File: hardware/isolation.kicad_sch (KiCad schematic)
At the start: 5 parts, among them IC2 UCC12040DVER

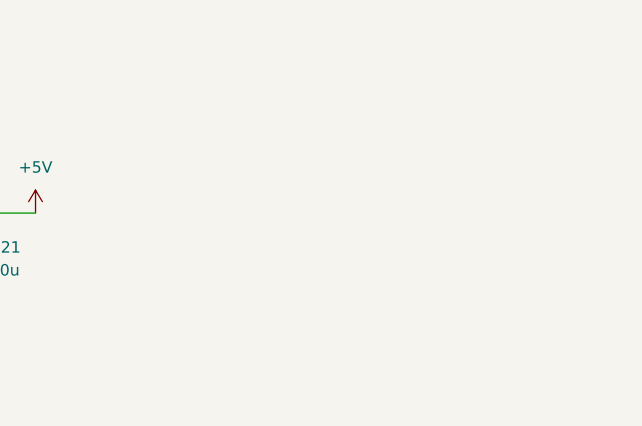
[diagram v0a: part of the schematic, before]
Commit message: Added 3V3-1 LDO
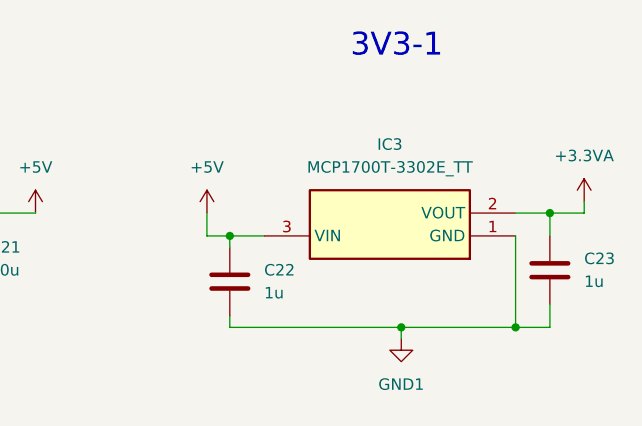
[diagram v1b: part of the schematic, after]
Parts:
- added C22, C23: 1u, Capacitor_SMD:C_0402_1005Metric, symbol Device:C
- added IC3: MCP1700T-3302E_TT, Stuttgart:SOT95P237X112-3N, symbol Stuttgart:MCP1700T-3302E_TT
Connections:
- net +5V: now also C22.1, IC3.3 (VIN)
- net GND1: now also C22.2, C23.2, IC3.1 (GND)
- new net +3.3VA: C23.1, IC3.2 (VOUT)
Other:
- note added: "3V3-1"

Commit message: Further ISO bridge development
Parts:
- added C24, C25: 100n, Capacitor_SMD:C_0402_1005Metric, symbol Device:C
- added IC4: ISO7742DBQR, Stuttgart:SOP64P600X175-16N, symbol Stuttgart:ISO7742DBQR
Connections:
- net +3.3VA: now also C25.1, IC4.10 (EN2), IC4.16 (VCC2)
- net GND: now also C24.2, IC4.2 (GND1_1), IC4.8 (GND1_2)
- net GND1: now also C25.2, IC4.15 (GND2_2), IC4.9 (GND2_1)
- new net +3V3: C24.1, IC4.1 (VCC1), IC4.7 (EN1)
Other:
- note added: "SPI Bridge 0"

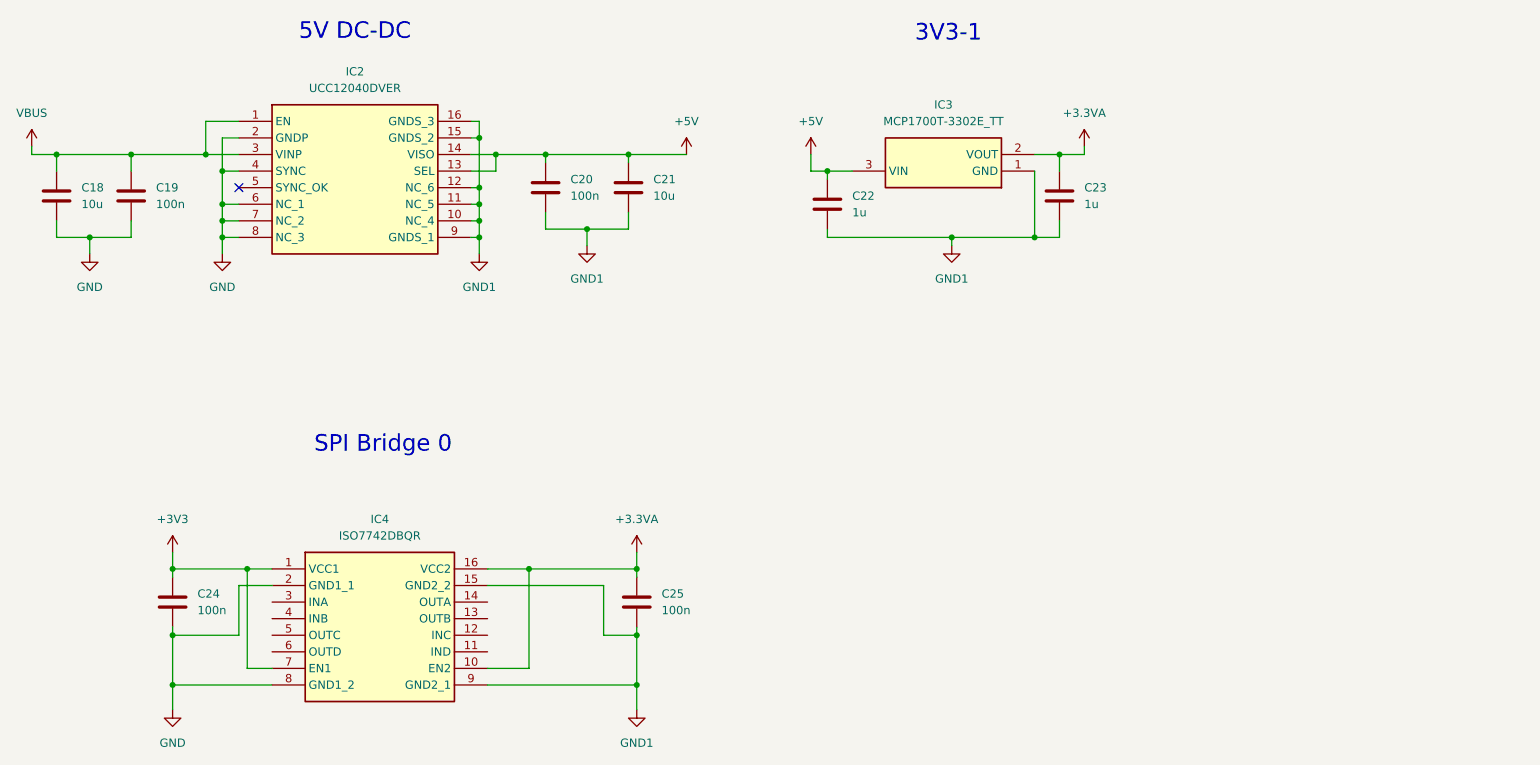
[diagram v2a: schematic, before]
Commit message: Isolation bridges complete
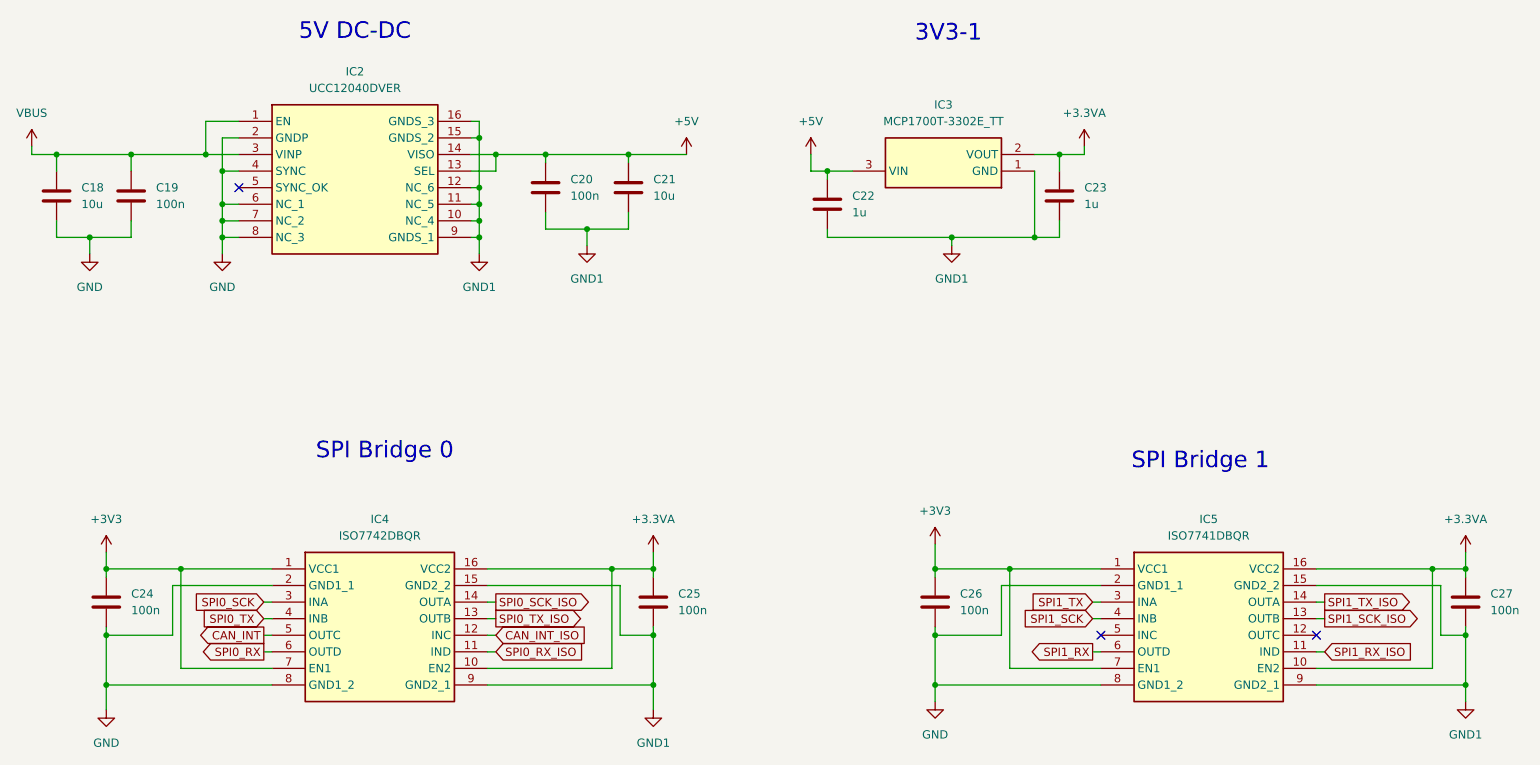
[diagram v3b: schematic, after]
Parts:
- added C26, C27: 100n, Capacitor_SMD:C_0402_1005Metric, symbol Device:C
- added IC5: ISO7741DBQR, Stuttgart:SOP64P600X175-16N, symbol Stuttgart:ISO7741DBQR
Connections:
- net +3.3VA: now also C27.1, IC5.10 (EN2), IC5.16 (VCC2)
- net +3V3: now also C26.1, IC5.1 (VCC1), IC5.7 (EN1)
- net GND: now also C26.2, IC5.2 (GND1_1), IC5.8 (GND1_2)
- net GND1: now also C27.2, IC5.15 (GND2_2), IC5.9 (GND2_1)
- net SPI0_RX_ISO: now reaches IC4.11 (IND)
- net CAN_INT_ISO: now reaches IC4.12 (INC)
- net SPI0_TX_ISO: now reaches IC4.13 (OUTB)
- net SPI0_SCK_ISO: now reaches IC4.14 (OUTA)
- net SPI0_SCK: now reaches IC4.3 (INA)
- net SPI0_TX: now reaches IC4.4 (INB)
- net CAN_INT: now reaches IC4.5 (OUTC)
- net SPI0_RX: now reaches IC4.6 (OUTD)
- new net SPI1_RX: IC5.6 (OUTD)
- new net SPI1_RX_ISO: IC5.11 (IND)
- new net SPI1_SCK: IC5.4 (INB)
- new net SPI1_SCK_ISO: IC5.13 (OUTB)
- new net SPI1_TX: IC5.3 (INA)
- new net SPI1_TX_ISO: IC5.14 (OUTA)
- no-connect marks 1 -> 3
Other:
- note added: "SPI Bridge 1"
- moved on the sheet: C24, C25

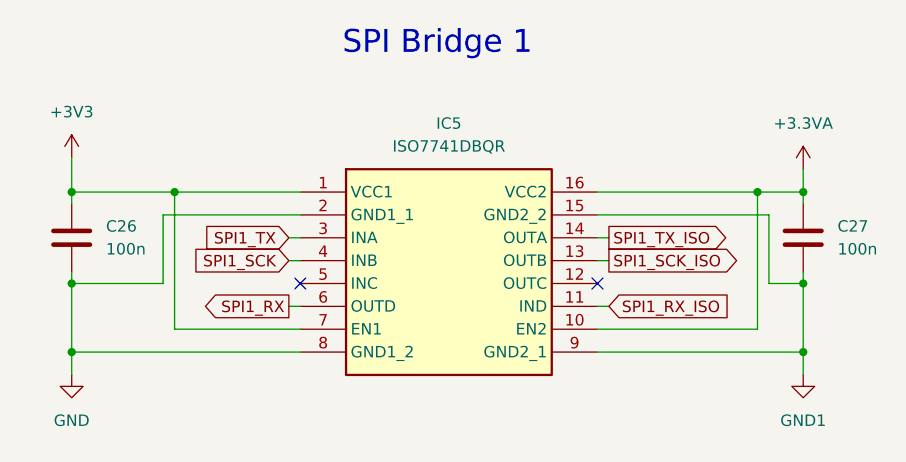
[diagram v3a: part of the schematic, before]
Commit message: CAN ADC on the board
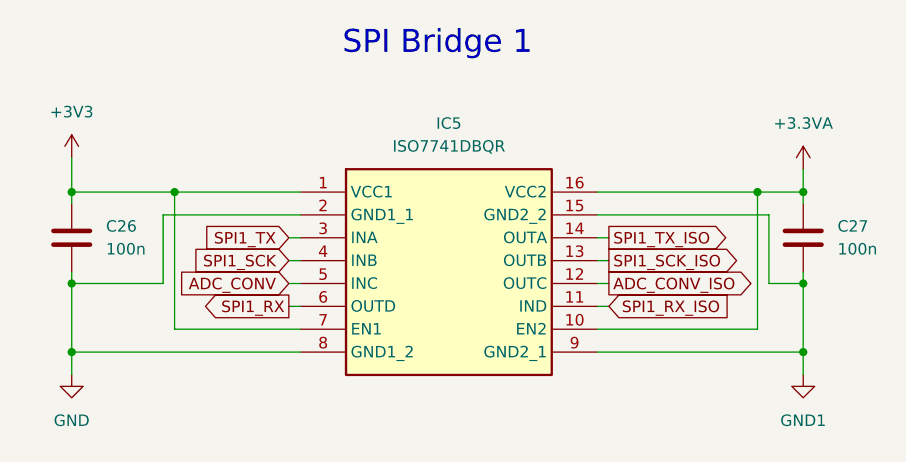
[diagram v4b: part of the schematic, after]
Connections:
- net ADC_CONV_ISO: now reaches IC5.12 (OUTC)
- net ADC_CONV: now reaches IC5.5 (INC)
- no-connect marks 3 -> 1
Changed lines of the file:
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@@
-	)
-	(no_connect
-		(at 190.5 114.3)
-	)
-	(no_connect
-		(at 223.52 114.3)
 	)
 	(no_connect
@@
 	(wire
 		(pts
+			(xy 189.23 114.3) (xy 190.5 114.3)
+		)
+		(stroke
+			(width 0)
+			(type default)
+		)
+	)
+	(wire
+		(pts
 			(xy 165.1 121.92) (xy 165.1 114.3)
 		)
@@
 	(wire
 		(pts
+			(xy 223.52 114.3) (xy 224.79 114.3)
+		)
+		(stroke
+			(width 0)
+			(type default)
+		)
+	)
+	(wire
+		(pts
 			(xy 223.52 109.22) (xy 224.79 109.22)
 		)
@@
 			(width 0)
 			(type default)
+		)
+	)
+	(global_label "ADC_CONV_ISO"
+		(shape output)
+		(at 224.79 114.3 0)
+		(fields_autoplaced yes)
+		(effects
+			(font
+				(size 1.27 1.27)
+			)
+			(justify left)
+		)
+		(property "Intersheetrefs" "${INTERSHEET_REFS}"
+			(at 241.5034 114.3 0)
+			(hide yes)
+			(show_name no)
+			(do_not_autoplace no)
+			(effects
+				(font
+					(size 1.27 1.27)
+				)
+				(justify left)
+			)
 		)
 	)
@@
 			(hide yes)
 			(show_name no)
+			(do_not_autoplace no)
+			(effects
+				(font
+					(size 1.27 1.27)
+				)
+				(justify right)
+			)
+		)
+	)
+	(global_label "ADC_CONV"
+		(shape input)
+		(at 189.23 114.3 180)
+		(fields_autoplaced yes)
+		(effects
+			(font
+				(size 1.27 1.27)
+			)
+			(justify right)
+		)
+		(property "Intersheetrefs" "${INTERSHEET_REFS}"
+			(at 176.629 114.3 0)
+			(hide yes)
+			(show_name no)

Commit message: Further iso bridge development
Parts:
- removed IC4: ISO7742DBQR, Stuttgart:SOP64P600X175-16N, symbol Stuttgart:ISO7742DBQR
- added IC4: ISO7763DBQR, Stuttgart:SOP64P600X175-16N, symbol Stuttgart:ISO7763DBQR
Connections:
- net +3.3VA: now also IC4.16 (VCC2)
- net +3V3: now also IC4.1 (VCC1)
- net CAN_INT: now also IC4.6 (OUTE)
- net CAN_INT_ISO: now also IC4.11 (INE)
- net GND: now also IC4.8 (GND1)
- net GND1: now also IC4.9 (GND2)
- net SPI0_RX: now also IC4.5 (OUTD)
- net SPI0_RX_ISO: now also IC4.12 (IND)
- net SPI0_SCK: now also IC4.2 (INA)
- net SPI0_SCK_ISO: now also IC4.15 (OUTA)
- net SPI0_TX: now also IC4.3 (INB)
- net SPI0_TX_ISO: now also IC4.14 (OUTB)
- net ADC_CONV renamed SPI1_CS
- net ADC_CONV_ISO renamed SPI1_CS_ISO
- new net CAN_INT1: IC4.7 (OUTF)
- new net CAN_INT1_ISO: IC4.10 (INF)
- new net SPI0_CS: IC4.4 (INC)
- new net SPI0_CS_ISO: IC4.13 (OUTC)

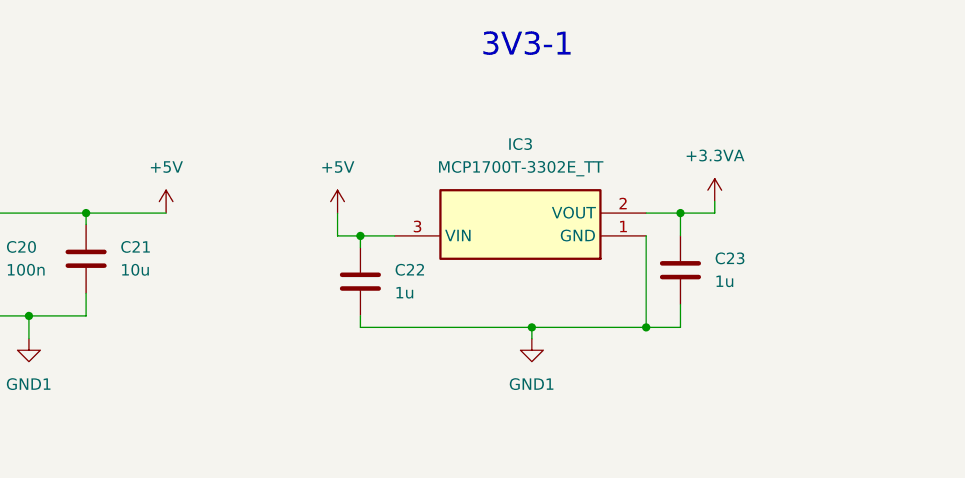
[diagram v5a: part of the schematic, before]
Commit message: Completed ADC, new components and test points
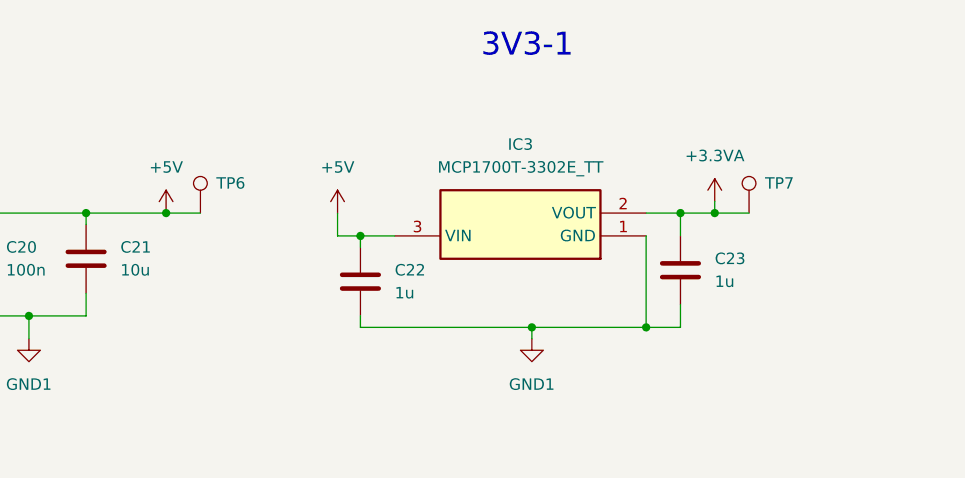
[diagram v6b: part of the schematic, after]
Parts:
- added TP6, TP7: TestPoint, TestPoint:TestPoint_Pad_D1.0mm, symbol Connector:TestPoint
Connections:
- net +3.3VA: now also TP7.1
- net +5V: now also TP6.1
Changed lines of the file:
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@@
 	)
 	(junction
+		(at 127 40.64)
+		(diameter 0)
+		(color 0 0 0 0)
+	)
+	(junction
 		(at 176.53 104.14)
 		(diameter 0)
@@
 	)
 	(junction
+		(at 187.96 40.64)
+		(diameter 0)
+		(color 0 0 0 0)
+	)
+	(junction
 		(at 53.34 40.64)
 		(diameter 0)
@@
 	(wire
 		(pts
+			(xy 187.96 40.64) (xy 191.77 40.64)
+		)
+		(stroke
+			(width 0)
+			(type default)
+		)
+	)
+	(wire
+		(pts
 			(xy 189.23 109.22) (xy 190.5 109.22)
 		)
@@
 	(wire
 		(pts
+			(xy 127 40.64) (xy 130.81 40.64)
+		)
+		(stroke
+			(width 0)
+			(type default)
+		)
+	)
+	(wire
+		(pts
 			(xy 64.77 119.38) (xy 66.04 119.38)
 		)
@@
 	)
 	(symbol
+		(lib_id "Connector:TestPoint")
+		(at 191.77 40.64 0)
+		(unit 1)
+		(body_style 1)
+		(exclude_from_sim no)
+		(in_bom yes)
+		(on_board yes)
+		(in_pos_files yes)
+		(dnp no)
+		(property "Reference" "TP7"
+			(at 193.548 37.338 0)
+			(show_name no)
+			(do_not_autoplace no)
+			(effects
+				(font
+					(size 1.27 1.27)
+				)
+				(justify left)
+			)
+		)
+		(property "Value" "TestPoint"
+			(at 194.31 38.6079 0)
+			(hide yes)
+			(show_name no)
+			(do_not_autoplace no)
+			(effects
+				(font
+					(size 1.27 1.27)
+				)
+				(justify left)
+			)
+		)
+		(property "Footprint" "TestPoint:TestPoint_Pad_D1.0mm"
+			(at 196.85 40.64 0)
+			(hide yes)
+			(show_name no)
+			(do_not_autoplace no)
+			(effects
+				(font
+					(size 1.27 1.27)
+				)
+			)
+		)
+		(property "Datasheet" ""
+			(at 196.85 40.64 0)
+			(hide yes)
+			(show_name no)
+			(do_not_autoplace no)
+			(effects
+				(font
+					(size 1.27 1.27)
+				)
+			)
+		)
+		(property "Description" "test point"
+			(at 191.77 40.64 0)
+			(hide yes)
+			(show_name no)
+			(do_not_autoplace no)
+			(effects
+				(font
+					(size 1.27 1.27)
+				)
+			)
+		)
+		(pin "1"
+		)
+		(instances
+			(project "Stuttgart"
+				(path "/6d354744-ce95-4d5c-b7ae-1990dae66f7b/ffc4b0bd-0ab0-410f-aa83-d070eecc8dc1"
+					(reference "TP7")
+					(unit 1)
+				)
+			)
+		)
+	)
+	(symbol
 		(lib_id "Device:C")
 		(at 121.92 109.22 0)
@@
 					(unit 1)
 				)
+			)
+		)
+	)
+	(symbol
+		(lib_id "Connector:TestPoint")
+		(at 130.81 40.64 0)
+		(unit 1)
+		(body_style 1)
+		(exclude_from_sim no)
+		(in_bom yes)
+		(on_board yes)
+		(in_pos_files yes)
+		(dnp no)
+		(property "Reference" "TP6"
+			(at 132.588 37.338 0)
+			(show_name no)
+			(do_not_autoplace no)
+			(effects
+				(font
+					(size 1.27 1.27)
+				)
+				(justify left)
+			)
+		)
+		(property "Value" "TestPoint"
+			(at 133.35 38.6079 0)
+			(hide yes)
+			(show_name no)
+			(do_not_autoplace no)
+			(effects
+				(font
+					(size 1.27 1.27)
+				)
+				(justify left)
+			)
+		)
+		(property "Footprint" "TestPoint:TestPoint_Pad_D1.0mm"
+			(at 135.89 40.64 0)
+			(hide yes)
+			(show_name no)
+			(do_not_autoplace no)
+			(effects
+				(font
+					(size 1.27 1.27)
+				)
+			)
+		)
+		(property "Datasheet" ""
+			(at 135.89 40.64 0)
+			(hide yes)
+			(show_name no)
+			(do_not_autoplace no)
+			(effects
+				(font
+					(size 1.27 1.27)
+				)
+			)
+		)
+		(property "Description" "test point"
+			(at 130.81 40.64 0)
+			(hide yes)
+			(show_name no)
+			(do_not_autoplace no)
+			(effects
+				(font
+					(size 1.27 1.27)
+				)
+			)
+		)
+		(pin "1"
+		)
+		(instances
+			(project "Stuttgart"
+				(path "/6d354744-ce95-4d5c-b7ae-1990dae66f7b/ffc4b0bd-0ab0-410f-aa83-d070eecc8dc1"
+					(reference "TP6")
+					(unit 1)
+				)
